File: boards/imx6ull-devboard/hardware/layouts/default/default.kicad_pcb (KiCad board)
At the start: 2 copper layers, 119 parts, among them Q1 Vgs ℝ+V

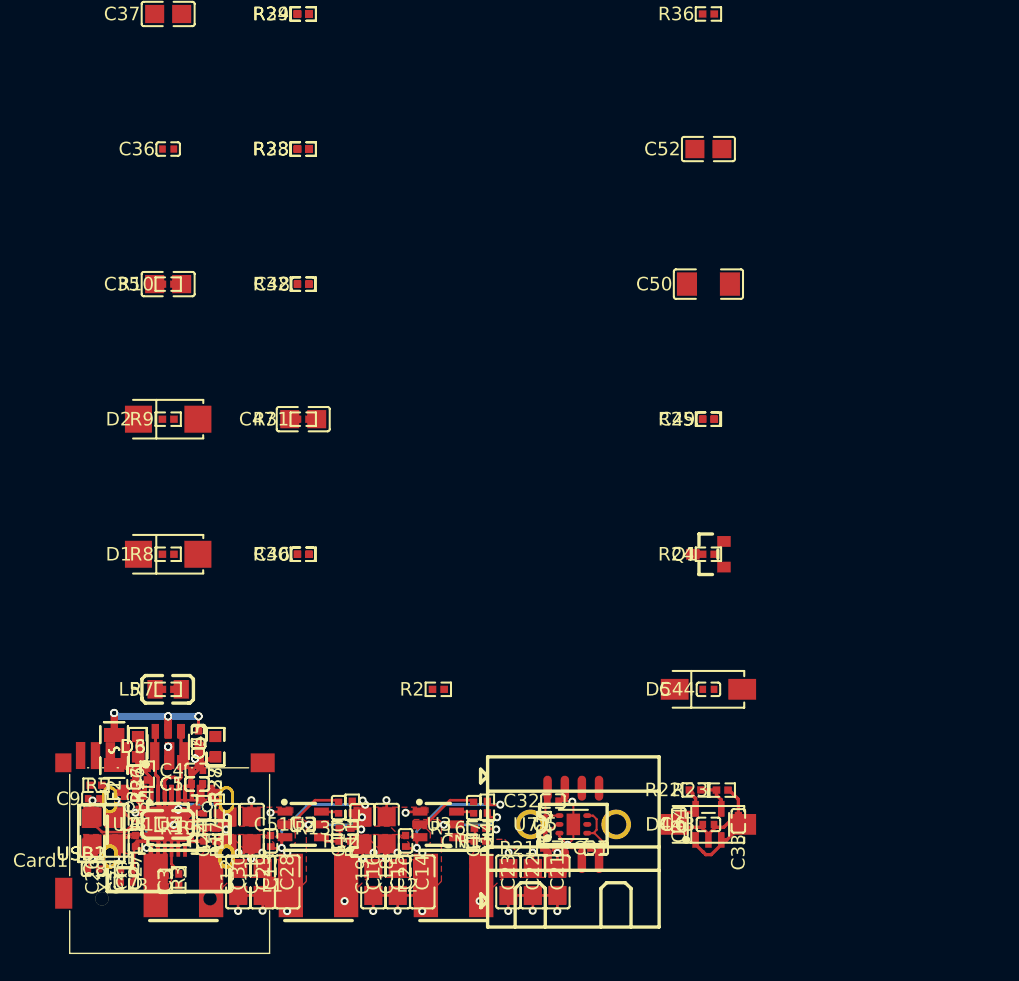
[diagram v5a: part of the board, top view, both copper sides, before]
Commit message: Debug subsystem v0 — JTAG, reset, boot DIP, LEDs, coin cell, headers
Components:
- 10-pin Cortex JTAG/SWD SMD header (Wcon, 1.27mm) with named pins
  per ARM debug spec (VTREF/SWDIO_TMS/SWCLK_TCK/SWO_TDO/TDI/NSRST/GNDs)
- SMD tactile reset button (XKB, JLC Basic) + 10kΩ pullup + 100nF debounce
- 2-position SMD DIP for BOOT_MODE[1:0] selection (kangshen DSIC02LSGET)
  with truth table documented; default position = SD boot
- 2x status LEDs (3V3 power-good always-on, MPU-driven heartbeat) via
  bridge pattern: power_3v3.hv ~> R ~> LED ~> power_3v3.lv
- CR2032 coin cell holder (Q&J) + 1kΩ charge limit → PowerTree.vbat_in
- 4-pin TTL UART header (atopile/pin-headers Male_2_54mm_1x4P_TH) for
  USB-TTL dongle fallback to MPU UART2
- 2-pin speaker header (atopile/pin-headers Male_2_54mm_1x2P_TH)

Atomic parts: added signal names to bare-pin parts (DIBO terminal block,
Wcon JTAG header, DSIC02LSGET DIP, Q&J cell holder) so they're accessible
from outside via .NAME instead of needing pin-number syntax.

Build clean. 6/9 subsystems landed.

Co-Authored-By: Claude Opus 4.7 (1M context) <noreply@anthropic.com>
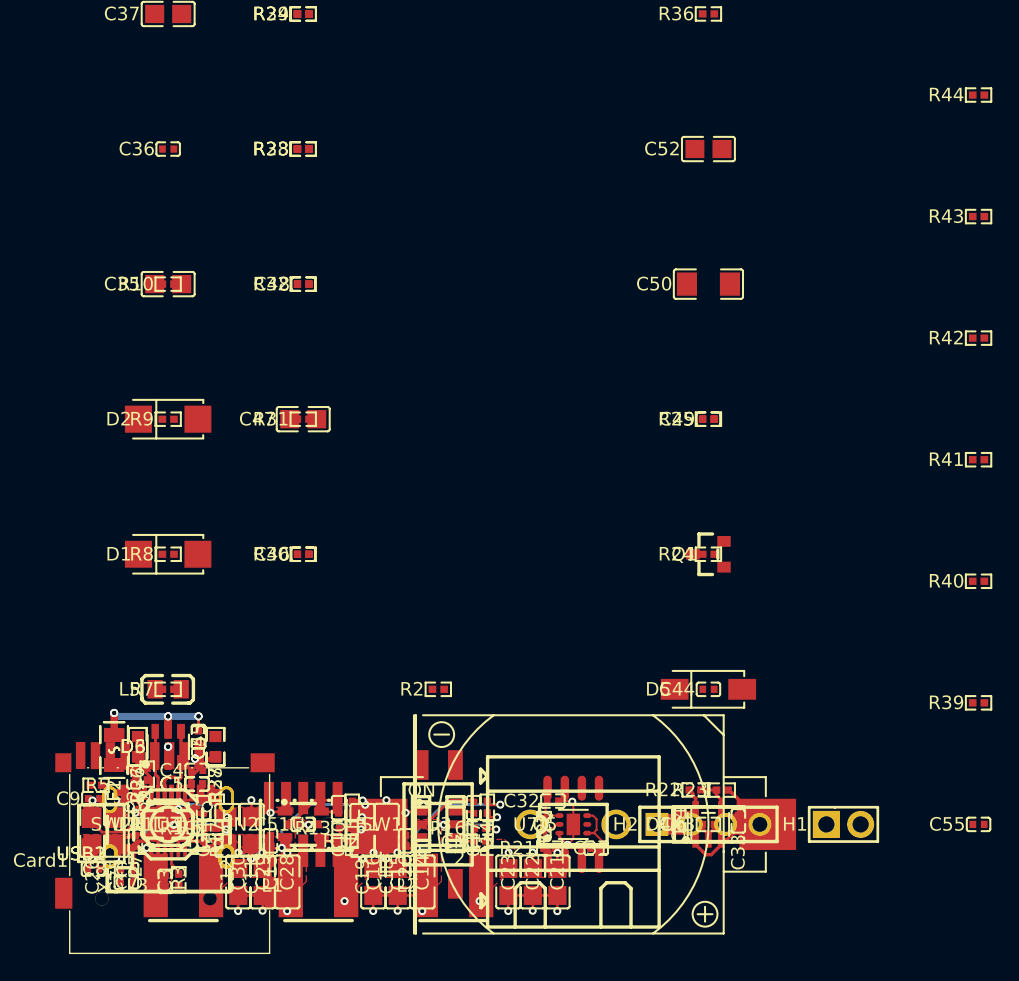
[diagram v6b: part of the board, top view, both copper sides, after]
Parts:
- added B1: , Q_J_CR2032_BS_6_1:BAT-TH_CR2032-BS-6-1, F.Cu at (30.0, 0.00)
- added C55: 100nF ±10%, Samsung_Electro_Mechanics_CL05B104KO5NNNC:C0402, F.Cu at (60.0, 0.00)
- added CN2: , Wcon_1310_1205G0M061CR02:CONN-SMD_1310-1205G0M061CR02, F.Cu at (10.0, 0.00)
- added H1: , XFCN_PZ254V_11_02P:HDR-TH_2P-P2.54-V-M, F.Cu at (50.0, 0.00)
- added H2: , Shenzhen_Kinghelm_Elec_KH_2_54PH180_1X4P_L11_5:HDR-TH_4P-P2.54-V-M, F.Cu at (40.0, 0.00)
- added R39: 10kΩ ±1%, UNI_ROYAL_0402WGF1002TCE:R0402, F.Cu at (60.0, -9.00)
- added R40: 10kΩ ±1%, UNI_ROYAL_0402WGF1002TCE:R0402, F.Cu at (60.0, -18.0)
- added R41: 1kΩ ±1%, UNI_ROYAL_0402WGF1001TCE:R0402, F.Cu at (60.0, -27.0)
- added R42: 680Ω ±1%, UNI_ROYAL_0402WGF6800TCE:R0402, F.Cu at (60.0, -36.0)
- added R43: 680Ω ±1%, UNI_ROYAL_0402WGF6800TCE:R0402, F.Cu at (60.0, -45.0)
- added R44: 10kΩ ±1%, UNI_ROYAL_0402WGF1002TCE:R0402, F.Cu at (60.0, -54.0)
- added SW1: , kangshen_DSIC02LSGET:SW-SMD_DSIC02LSGET, F.Cu at (20.0, 0.00)
- added SW2: , XKB_Connectivity_TS_1187A_B_A_B:SW-SMD_4P-L5.1-W5.1-P3.70-LS6.5-TL_H1.5, F.Cu at (0.00, 0.00)
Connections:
- net POS renamed pin_in-POS
- net anode renamed or_bench-anode
- net line renamed _reset-line
- C1 pad 2: lv -> cathode
- C11 pad 1: cathode -> power_5v-cathode
- C11 pad 2: lv -> cathode
- C12 pad 1: cathode -> power_5v-cathode
- C12 pad 2: lv -> cathode
- C13 pad 1: cathode -> power_5v-cathode
- C13 pad 2: lv -> cathode
- C14 pad 2: lv -> cathode
- C15 pad 2: lv -> cathode
- C16 pad 2: lv -> cathode
- C18 pad 1: cathode -> power_5v-cathode
- C18 pad 2: lv -> cathode
- C19 pad 1: cathode -> power_5v-cathode
- C19 pad 2: lv -> cathode
- C2 pad 2: lv -> cathode
- C20 pad 1: cathode -> power_5v-cathode
- C20 pad 2: lv -> cathode
- C21 pad 2: lv -> cathode
- C22 pad 2: lv -> cathode
- C23 pad 2: lv -> cathode
- C25 pad 1: cathode -> power_5v-cathode
- C25 pad 2: lv -> cathode
- C26 pad 1: cathode -> power_5v-cathode
- C26 pad 2: lv -> cathode
- C27 pad 1: cathode -> power_5v-cathode
- C27 pad 2: lv -> cathode
- C28 pad 2: lv -> cathode
- C29 pad 2: lv -> cathode
- C3 pad 2: lv -> cathode
- C30 pad 2: lv -> cathode
- C31 pad 2: lv -> cathode
- C33 pad 1: cathode -> power_5v-cathode
- C33 pad 2: lv -> cathode
- C34 pad 2: vbat_in-lv -> lv
- C35 pad 2: lv -> cathode
- C36 pad 2: lv -> cathode
- C37 pad 2: vbat_in-lv -> lv
- C38 pad 2: lv -> cathode
- C39 pad 2: lv -> cathode
- C4 pad 2: lv -> cathode
- C40 pad 2: lv -> cathode
- C41 pad 2: lv -> cathode
- C42 pad 2: lv -> cathode
- C43 pad 2: lv -> cathode
- C44 pad 1: cathode -> power_5v-cathode
- C44 pad 2: lv -> cathode
- C45 pad 2: lv -> cathode
- C46 pad 2: lv -> cathode
- C47 pad 2: lv -> cathode
- C48 pad 2: lv -> cathode
- C49 pad 1: cathode -> power_5v-cathode
- C49 pad 2: lv -> cathode
- C5 pad 2: lv -> cathode
- C50 pad 1: cathode -> power_5v-cathode
- C50 pad 2: lv -> cathode
- C51 pad 2: lv -> cathode
- C52 pad 1: cathode -> power_5v-cathode
- C52 pad 2: lv -> cathode
- C53 pad 2: lv -> cathode
- C54 pad 2: lv -> cathode
- C6 pad 2: lv -> cathode
- C7 pad 2: lv -> cathode
- C8 pad 2: lv -> cathode
- C9 pad 2: lv -> cathode
- CN1 pad 2: lv -> cathode
- Card1 pad 10: lv -> cathode
- Card1 pad 11: lv -> cathode
- Card1 pad 12: lv -> cathode
- Card1 pad 13: lv -> cathode
- Card1 pad 6: lv -> cathode
- D3 pad 2: lv -> cathode
- D4 pad 2: cathode -> power_5v-cathode
- D5 pad 2: cathode -> power_5v-cathode
- D6 pad 2: lv -> cathode
- R1 pad 2: lv -> cathode
- R11 pad 2: cathode -> power_5v-cathode
- R13 pad 2: lv -> cathode
- R14 pad 2: cathode -> power_5v-cathode
- R16 pad 2: lv -> cathode
- R17 pad 2: cathode -> power_5v-cathode
- R19 pad 2: lv -> cathode
- R23 pad 2: vbat_in-lv -> lv
- R26 pad 2: lv -> cathode
- R27 pad 2: lv -> cathode
- R28 pad 2: lv -> cathode
- R3 pad 2: lv -> cathode
- R36 pad 2: lv -> cathode
- R37 pad 2: lv -> cathode
- R38 pad 2: lv -> cathode
- R4 pad 2: lv -> cathode
- R5 pad 2: lv -> cathode
- U1 pad 25: lv -> cathode
- U2 pad 1: lv -> cathode
- U2 pad 3: cathode -> power_5v-cathode
- U3 pad 1: lv -> cathode
- U3 pad 3: cathode -> power_5v-cathode
- U4 pad 1: lv -> cathode
- U4 pad 3: cathode -> power_5v-cathode
- U5 pad 3: lv -> cathode
- U6 pad 1: cathode -> power_5v-cathode
- U6 pad 2: lv -> cathode
- U6 pad 3: cathode -> power_5v-cathode
- U7 pad 3: lv -> cathode
- U7 pad 5: cathode -> power_5v-cathode
- U8 pad 10: speaker_n_pad -> speaker_n
- U8 pad 11: lv -> cathode
- U8 pad 15: lv -> cathode
- U8 pad 17: lv -> cathode
- U8 pad 3: lv -> cathode
- U8 pad 9: speaker_p_pad -> speaker_p
- USB1 pad 1: lv -> cathode
- USB1 pad 12: lv -> cathode
- USB1 pad 13: lv -> cathode
- USB1 pad 14: lv -> cathode
- USB1 pad 15: lv -> cathode
- USB1 pad 16: lv -> cathode
- USB2 pad 1: lv -> cathode
- USB2 pad 12: lv -> cathode
- USB2 pad 13: lv -> cathode
- USB2 pad 14: lv -> cathode
- USB2 pad 15: lv -> cathode
- USB2 pad 16: lv -> cathode
- X1 pad 2: lv -> cathode
- X1 pad 4: lv -> cathode
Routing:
- net lv: track 21.2 -> 0.00 mm
- net cathode: track 0.00 -> 21.2 mm

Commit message: WIP: i.MX 6ULL MPU module — pinmux verified + Board wired, build blocked on picker
MPU module written with research-verified pinmux assignments (NOT guesses):
  - SAI3 on LCD_HSYNC/ENABLE/RESET (NOT SAI2 — SAI2 only muxes to JTAG or SD1
    pads on i.MX 6ULL, would kill JTAG or USDHC1)
  - MDIO/MDC on UART1_CTS_B/RTS_B (K15/J14) per imx6ul-pinfunc.h
  - SD_CD on GPIO1_IO09 (M15)
  - ETH_PHY_RESET on GPIO1_IO02 with 10kΩ pulldown (PHY held in reset until firmware)
  - JTAG_MOD via 4.7kΩ to GND (RM §59 Secure JTAG normal mode)
  - TEST_MODE via 1kΩ to GND (mandatory)
  - ONOFF + POR_B pull-ups to VDD_SNVS_IN (NOT 3V3 — SNVS-domain inputs)
  - USB_OTG1_VBUS divider (20k/30k → ~3V) per datasheet §6.4.4 protection
  - DRAM_VREF = NVCC_DRAM/2 via 1k/1k 1% divider + 100nF + 10nF filter caps
  - DRAM_ZQPAD via 240Ω 1% to GND

Board top-level wires MPU to all 7 existing subsystems:
  - PowerTree provides 4 rails (3V3, 1V4_arm, 1V4_soc, 1V35, SNVS)
  - Network/USDHC/Audio/USBUart/Debug all connected to MPU buses

DDR3 bus exposed as DDR3Bus interface; awaits DDR3 SDRAM module.

Sources cited in mpu.ato comments:
  - IMX6ULLIEC datasheet Tables 82, 94, 95
  - Mainline Linux imx6ul-pinfunc.h
  - imx6ul-14x14-evk.dtsi reference

KNOWN BLOCKER: ato build fails with picker contradiction on
  Board.psu.buck_3v3.feedback_divider.chain.resistors[0/1].resistance
even with explicit pinned R values. This is an atopile internal solver issue —
the same module compiled fine with fewer downstream consumers but the larger
constraint set (MPU + 6 other subsystems referencing power_3v3) makes the
TPS563201 package's internal feedback divider unsatisfiable.

Stopping here for user direction rather than continuing to iterate on
constraints without root-cause understanding.

Co-Authored-By: Claude Opus 4.7 (1M context) <noreply@anthropic.com>
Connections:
- R39 pad 2: hv -> power_snvs-cathode
- R40 pad 2: hv -> power_snvs-cathode
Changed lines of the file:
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@@
 	(net 50 "power_1v4_soc-hv")
 	(net 51 "_ldo_snvs_out-anode")
-	(net 54 "power_snvs-cathode")
 	(net 15 "cap_v3-power-hv")
 	(net 35 "nRTS")
@@
 	(net 108 "lv")
 	(net 109 "vbat_in-anode")
+	(net 52 "power_snvs-cathode")
 	(footprint "Microchip_Tech_LAN8742A_CZ_TR:QFN-24_L4.0-W4.0-P0.50-TL-EP2.5"
 		(layer "F.Cu")
@@
 			(size 2 2)
 			(layers "F.Cu" "F.Paste" "F.Mask")
-			(net 54 "power_snvs-cathode")
+			(net 52 "power_snvs-cathode")
 		)
 		(embedded_fonts no)
@@
 			(size 2 2)
 			(layers "F.Cu" "F.Paste" "F.Mask")
-			(net 54 "power_snvs-cathode")
+			(net 52 "power_snvs-cathode")
 		)
 		(embedded_fonts no)
@@
 			(size 1.41 1.35)
 			(layers "F.Cu" "F.Paste" "F.Mask")
-			(net 54 "power_snvs-cathode")
+			(net 52 "power_snvs-cathode")
 		)
 		(embedded_fonts no)
@@
 		)
 		(pad "" thru_hole circle
-			(at -1.9 -0 0)
+			(at -1.9 -0)
 			(size 1.05 1.05)
 			(drill 1.05)
@@
 		)
 		(pad "" thru_hole circle
-			(at 1.9 -0 0)
+			(at 1.9 -0)
 			(size 1.05 1.05)
 			(drill 1.05)
@@
 		)
 		(pad "1" thru_hole rect
-			(at -1.27 0 0)
+			(at -1.27 0)
 			(size 2 2)
 			(drill 1.199998)
@@
 		)
 		(pad "2" thru_hole circle
-			(at 1.27 0 0)
+			(at 1.27 0)
 			(size 2 2)
 			(drill 1.199998)
@@
 			(size 0.57 0.54)
 			(layers "F.Cu" "F.Paste" "F.Mask")
-			(net 39 "hv")
+			(net 52 "power_snvs-cathode")
 		)
 		(pad "1" smd rect
@@
 			(size 0.57 0.54)
 			(layers "F.Cu" "F.Paste" "F.Mask")
-			(net 39 "hv")
+			(net 52 "power_snvs-cathode")
 		)
 		(pad "1" smd rect
@@
 	(group "dbg.hdr_spk"
 		(locked no)
-		(members "8d349a68-802b-450d-bfa1-fe594642524b")
+		(members "98f623f6-ef0b-4de6-83db-48de4642524b")
 	)
 )

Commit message: 🚀 BUILD SUCCESSFUL — 58-part Linux dev board in KiCad
All 14 build stages green. 1.26 MB default.kicad_pcb generated.

Two fixes that closed the build:

1. Net name collisions (segfault → crash):
   Set explicit override_net_name on top-level rails (VCC_5V, VCC_3V3,
   VCC_1V4_ARM, VCC_1V4_SOC, VCC_NVCC_DRAM, VCC_1V8, VCC_SNVS, VBAT, GND)
   in main.ato:Board. atopile's PCB writer was crashing when auto-derived
   net names like "hv"/"lv"/"cathode" collided across modules. Explicit
   names give the writer deterministic output and the segfault disappeared.

2. Broken MPU pin numbers (29 lines):
   The auto-generated NXP_Semicon_MCIMX6Y2CVM08AB part from `ato create part`
   had 29 pin assignments missing their BGA row letter (e.g.,
   `BOOT_MODE1 ~ pin 10` instead of `pin U10`, `DRAM_DATA01 ~ pin 6`
   instead of `pin U6`). Read pages 113-122 of the IMX6ULLIEC datasheet
   (Tables 90, 91, 92) and corrected all 29 to the actual BGA coordinates:

   - BOOT_MODE1=U10, CCM_PMIC_STBY_REQ=U9
   - DRAM_DATA01=U6, ..03=U7, ..04=U8, ..07=U4, ..08=U2, ..09=U3, ..10=U5, ..11=R4
   - DRAM_RESET=G4, NVCC_DRAM (6th)=G6
   - RTC_XTALO=U11, UART3_RTS_B=G14, UART5_RX_DATA=G13
   - USB_OTG1_CHD_B=U16, USB_OTG1_DP=U15
   - USB_OTG2_DP=U13, USB_OTG2_VBUS=U12
   - 10× VSS pin row letters: R17, U14, U17, G5, M11, M10, M9, M8, G15, R5
   - CSI_DATA03 was D18 (out of bounds — BGA only goes to col 17); fixed to E1

   These were genuine errors in EasyEDA's symbol import — datasheet was the
   ground truth. With pin numbers correct, the i.MX 6ULL appears in the
   BOM as U9 with the correct BGA-289 footprint.

Final BOM: 58 line items including
  - U1: LAN8742A Ethernet PHY
  - U2/U3/U4: 3× TPS563201 buck (commonized via local fork)
  - U5: TLV75901 LDO 1V8
  - U6: LDK220 LDO SNVS
  - U7: CH340N USB-UART
  - U8: MAX98357A I2S Class-D amp
  - U9: i.MX 6ULL MCIMX6Y2CVM08AB BGA-289
  - 2× USB-C, 2× SS54 + 2× SS34 OR Schottkys, 2× USBLC6 ESD, 2× ferrite beads
  - 9× 10kΩ commonized 0402, 4× 47kΩ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
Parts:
- added C56: 10µF ±10%, Samsung_Electro_Mechanics_CL21A106KAYNNNE:C0805, F.Cu at (10.0, 0.00)
- added C57: 10µF ±10%, Samsung_Electro_Mechanics_CL21A106KAYNNNE:C0805, F.Cu at (10.0, -6.00)
- added C58: 22µF ±20%, Samsung_Electro_Mechanics_CL21A226MAQNNNE:C0805, F.Cu at (10.0, -12.0)
- added C59: 1µF ±10%, Samsung_Electro_Mechanics_CL05A105KA5NQNC:C0402, F.Cu at (10.0, -18.0)
- added C60: 10µF ±10%, Samsung_Electro_Mechanics_CL21A106KAYNNNE:C0805, F.Cu at (10.0, -24.0)
- added C61: 1µF ±10%, Samsung_Electro_Mechanics_CL05A105KA5NQNC:C0402, F.Cu at (10.0, -30.0)
- added C62: 1µF ±10%, Samsung_Electro_Mechanics_CL05A105KA5NQNC:C0402, F.Cu at (10.0, -36.0)
- added C63: 1µF ±10%, Samsung_Electro_Mechanics_CL05A105KA5NQNC:C0402, F.Cu at (10.0, -42.0)
- added C64: 1µF ±10%, Samsung_Electro_Mechanics_CL05A105KA5NQNC:C0402, F.Cu at (10.0, -48.0)
- added C65: 100nF ±10%, Samsung_Electro_Mechanics_CL05B104KO5NNNC:C0402, F.Cu at (10.0, -54.0)
- added C66: 10nF ±10%, Samsung_Electro_Mechanics_CL05B103KB5NNNC:C0402, F.Cu at (10.0, -60.0)
- added C67: 22pF ±5%, FH_0402CG220J500NT:C0402, F.Cu at (10.0, -66.0)
- added C68: 22pF ±5%, FH_0402CG220J500NT:C0402, F.Cu at (10.0, -72.0)
- added C69: 100nF ±10%, Samsung_Electro_Mechanics_CL05B104KO5NNNC:C0402, F.Cu at (10.0, -78.0)
- added C70: 100nF ±10%, Samsung_Electro_Mechanics_CL05B104KO5NNNC:C0402, F.Cu at (10.0, -90.0)
- added C71: 100nF ±10%, Samsung_Electro_Mechanics_CL05B104KO5NNNC:C0402, F.Cu at (10.0, -96.0)
- added C72: 100nF ±10%, Samsung_Electro_Mechanics_CL05B104KO5NNNC:C0402, F.Cu at (10.0, -102.0)
- added C73: 100nF ±10%, Samsung_Electro_Mechanics_CL05B104KO5NNNC:C0402, F.Cu at (10.0, -108.0)
- added C74: 100nF ±10%, Samsung_Electro_Mechanics_CL05B104KO5NNNC:C0402, F.Cu at (10.0, -114.0)
- added C75: 100nF ±10%, Samsung_Electro_Mechanics_CL05B104KO5NNNC:C0402, F.Cu at (10.0, -120.0)
- added C76: 100nF ±10%, Samsung_Electro_Mechanics_CL05B104KO5NNNC:C0402, F.Cu at (10.0, -126.0)
- added C77: 100nF ±10%, Samsung_Electro_Mechanics_CL05B104KO5NNNC:C0402, F.Cu at (10.0, -132.0)
- added C78: 100nF ±10%, Samsung_Electro_Mechanics_CL05B104KO5NNNC:C0402, F.Cu at (10.0, -138.0)
- added C79: 100nF ±10%, Samsung_Electro_Mechanics_CL05B104KO5NNNC:C0402, F.Cu at (10.0, -84.0)
- added C80: 100nF ±10%, Samsung_Electro_Mechanics_CL05B104KO5NNNC:C0402, F.Cu at (10.0, -144.0)
- added C81: 100nF ±10%, Samsung_Electro_Mechanics_CL05B104KO5NNNC:C0402, F.Cu at (10.0, -150.0)
- added C82: 100nF ±10%, Samsung_Electro_Mechanics_CL05B104KO5NNNC:C0402, F.Cu at (10.0, -156.0)
- added C83: 100nF ±10%, Samsung_Electro_Mechanics_CL05B104KO5NNNC:C0402, F.Cu at (10.0, -162.0)
- added C84: 100nF ±10%, Samsung_Electro_Mechanics_CL05B104KO5NNNC:C0402, F.Cu at (10.0, -168.0)
- added C85: 100nF ±10%, Samsung_Electro_Mechanics_CL05B104KO5NNNC:C0402, F.Cu at (10.0, -174.0)
- added C86: 100nF ±10%, Samsung_Electro_Mechanics_CL05B104KO5NNNC:C0402, F.Cu at (10.0, -180.0)
- added C87: 100nF ±10%, Samsung_Electro_Mechanics_CL05B104KO5NNNC:C0402, F.Cu at (10.0, -186.0)
- added C88: 100nF ±10%, Samsung_Electro_Mechanics_CL05B104KO5NNNC:C0402, F.Cu at (10.0, -192.0)
- added C89: 100nF ±10%, Samsung_Electro_Mechanics_CL05B104KO5NNNC:C0402, F.Cu at (10.0, -198.0)
- added C90: 100nF ±10%, Samsung_Electro_Mechanics_CL05B104KO5NNNC:C0402, F.Cu at (10.0, -204.0)
- added C91: 100nF ±10%, Samsung_Electro_Mechanics_CL05B104KO5NNNC:C0402, F.Cu at (10.0, -210.0)
- added C92: 100nF ±10%, Samsung_Electro_Mechanics_CL05B104KO5NNNC:C0402, F.Cu at (10.0, -216.0)
- added R45: 30kΩ ±1%, UNI_ROYAL_0402WGF3002TCE:R0402, F.Cu at (10.0, -258.0)
- added R46: 20kΩ ±1%, UNI_ROYAL_0402WGF2002TCE:R0402, F.Cu at (10.0, -264.0)
- added R47: 1kΩ ±1%, UNI_ROYAL_0402WGF1001TCE:R0402, F.Cu at (10.0, -270.0)
- added R48: 1kΩ ±1%, UNI_ROYAL_0402WGF1001TCE:R0402, F.Cu at (10.0, -276.0)
- added R49: 240Ω ±1%, YAGEO_RC0402FR_07240RL:R0402, F.Cu at (10.0, -282.0)
- added R50: 10kΩ ±1%, UNI_ROYAL_0402WGF1002TCE:R0402, F.Cu at (10.0, -300.0)
- added R51: 8.2kΩ ±1%, UNI_ROYAL_0402WGF8201TCE:R0402, F.Cu at (10.0, -306.0)
- added R52: 10kΩ ±1%, UNI_ROYAL_0402WGF1002TCE:R0402, F.Cu at (10.0, -288.0)
- added R53: 7.5kΩ ±1%, UNI_ROYAL_0402WGF7501TCE:R0402, F.Cu at (10.0, -294.0)
- added R54: 10kΩ ±1%, UNI_ROYAL_0402WGF1002TCE:R0402, F.Cu at (10.0, -312.0)
- added R55: 33kΩ ±1%, UNI_ROYAL_0402WGF3302TCE:R0402, F.Cu at (10.0, -318.0)
- added U9: , NXP_Semicon_MCIMX6Y2CVM08AB:BGA-289_L14.0-W14.0-R17-C17-P0.80-BL, F.Cu at (0.00, 0.00)
- C14, C15, C16, C21, C22, C23, C28, C29, C30: value 10µF ±10% -> 100nF ±10%; footprint Samsung_Electro_Mechanics_CL21A106KAYNNNE:C0805 -> YAGEO_CC0603KRX7R9BB104:C0603
- L1, L2, L3: value L 1.54-2.86µH -> L 2.2µH ±20%; footprint SXN_SMNR5030_2R2N:IND-SMD_L5.0-W5.0_SMNR5030 -> cjiang_FXL0420_2R2_M:IND-SMD_L4.4-W4.2
- R12: value 13.3kΩ ±1% -> 4.7kΩ ±1%; footprint FOJAN_FRC0402F1332TS:R0402 -> UNI_ROYAL_0402WGF4701TCE:R0402
- R13, R15: value 16.2kΩ ±1% -> 10kΩ ±1%; footprint UNI_ROYAL_0402WGF1622TCE:R0402 -> UNI_ROYAL_0402WGF1002TCE:R0402
- R16: value 21.5kΩ ±1% -> 10kΩ ±1%; footprint UNI_ROYAL_0402WGF2152TCE:R0402 -> UNI_ROYAL_0402WGF1002TCE:R0402
- R18: value 10.2kΩ ±1% -> 1kΩ ±1%; footprint UNI_ROYAL_0402WGF1022TCE:R0402 -> UNI_ROYAL_0402WGF1001TCE:R0402
- R19: value 3.09kΩ ±1% -> 10kΩ ±1%; footprint Viking_Tech_ARG02FTC3091:R0402 -> UNI_ROYAL_0402WGF1002TCE:R0402
- moved R19 252.4 mm to (10.0, -252.0)
- moved R18 247.3 mm to (10.0, -246.0), turned to 0 degrees
- moved R16 240.6 mm to (10.0, -240.0)
- moved R15 235.6 mm to (10.0, -234.0), turned to 0 degrees
- moved R13 228.3 mm to (10.0, -228.0)
- moved R12 223.3 mm to (10.0, -222.0), turned to 0 degrees
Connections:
- net MDIO renamed UART1_RTS_B
- B1 pad 2: lv -> cathode
- C1 pad 1: hv -> power_3v3-cathode
- C11 pad 1: power_5v-cathode -> input_caps[0]-power-hv-1
- C11 pad 2: cathode -> input_caps[0]-power-lv-1
- C12 pad 1: power_5v-cathode -> input_caps[1]-power-hv-1
- C12 pad 2: cathode -> input_caps[1]-power-lv-1
- C13 pad 1: power_5v-cathode -> input_caps[2]-power-hv-1
- C13 pad 2: cathode -> input_caps[2]-power-lv-1
- C14 pad 1: power_1v4_arm-hv -> output_caps[0]-power-hv-1
- C14 pad 2: cathode -> output_caps[0]-power-lv-1
- C15 pad 1: power_1v4_arm-hv -> output_caps[1]-power-hv-1
- C15 pad 2: cathode -> output_caps[1]-power-lv-1
- C16 pad 1: power_1v4_arm-hv -> output_caps[2]-power-hv-1
- C16 pad 2: cathode -> output_caps[2]-power-lv-1
- C18 pad 1: power_5v-cathode -> input_caps[0]-power-hv
- C18 pad 2: cathode -> input_caps[0]-power-lv
- C19 pad 1: power_5v-cathode -> input_caps[1]-power-hv
- C19 pad 2: cathode -> input_caps[1]-power-lv
- C2 pad 1: hv -> power_3v3-cathode
- C20 pad 1: power_5v-cathode -> input_caps[2]-power-hv
- C20 pad 2: cathode -> input_caps[2]-power-lv
- C21 pad 1: _buck_1v35_out-hv -> output_caps[0]-power-hv
- C21 pad 2: cathode -> output_caps[0]-power-lv
- C22 pad 1: _buck_1v35_out-hv -> output_caps[1]-power-hv
- C22 pad 2: cathode -> output_caps[1]-power-lv
- C23 pad 1: _buck_1v35_out-hv -> output_caps[2]-power-hv
- C23 pad 2: cathode -> output_caps[2]-power-lv
- C25 pad 1: power_5v-cathode -> input_caps[0]-power-hv-2
- C25 pad 2: cathode -> input_caps[0]-power-lv-2
- C26 pad 1: power_5v-cathode -> input_caps[1]-power-hv-2
- C26 pad 2: cathode -> input_caps[1]-power-lv-2
- C27 pad 1: power_5v-cathode -> input_caps[2]-power-hv-2
- C27 pad 2: cathode -> input_caps[2]-power-lv-2
- C28 pad 1: hv -> output_caps[0]-power-hv-2
- C28 pad 2: cathode -> output_caps[0]-power-lv-2
- C29 pad 1: hv -> output_caps[1]-power-hv-2
- C29 pad 2: cathode -> output_caps[1]-power-lv-2
- C3 pad 1: hv -> power_3v3-cathode
- C30 pad 1: hv -> output_caps[2]-power-hv-2
- C30 pad 2: cathode -> output_caps[2]-power-lv-2
- C31 pad 1: hv -> power_3v3-cathode
- C32 pad 2: power_1v8-lv -> lv
- C34 pad 2: lv -> cathode
- C37 pad 1: power_snvs-cathode -> power_3v3-cathode
- C37 pad 2: lv -> cathode
- C4 pad 1: hv -> power_3v3-cathode
- C43 pad 1: cap_v3-power-hv -> hv
- C46 pad 1: hv -> power_3v3-cathode
- C47 pad 1: hv -> power_3v3-cathode
- C48 pad 1: hv -> power_3v3-cathode
- C5 pad 1: hv -> power_3v3-cathode
- C51 pad 1: hv -> power_3v3-cathode
- C54 pad 1: hv -> power_3v3-cathode
- CN2 pad 1: hv -> power_3v3-cathode
- Card1 pad 4: hv -> power_3v3-cathode
- D1 pad 1: power_snvs-cathode -> power_3v3-cathode
- D2 pad 1: power_snvs-cathode -> power_3v3-cathode
- H2 pad 2: hv -> power_3v3-cathode
- H2 pad 3: uart_console-TX -> TX
- H2 pad 4: uart_console-RX -> RX
- L3 pad 2: hv -> power_3v3-cathode
- R10 pad 2: hv -> power_3v3-cathode
- R12 pad 1: power_1v4_arm-hv -> JTAG_MOD
- R12 pad 2: feedback_divider-ref_out-hv-1 -> cathode
- R13 pad 1: feedback_divider-ref_out-hv-1 -> ONOFF
- R13 pad 2: cathode -> power_3v3-cathode
- R15 pad 1: _buck_1v35_out-hv -> _reset-line
- R15 pad 2: feedback_divider-ref_out-hv -> cathode
- R16 pad 1: feedback_divider-ref_out-hv -> c_rst_db-power-hv
- R16 pad 2: cathode -> power_3v3-cathode
- R18 pad 1: hv -> TEST_MODE
- R18 pad 2: feedback_divider-ref_out-hv-2 -> cathode
- R19 pad 1: feedback_divider-ref_out-hv-2 -> N_TRST
- R19 pad 2: cathode -> power_3v3-cathode
- R2 pad 2: hv -> power_3v3-cathode
- R20 pad 2: feedback_divider-ref_out-hv-3 -> feedback_divider-ref_out-hv
- R21 pad 1: feedback_divider-ref_out-hv-3 -> feedback_divider-ref_out-hv
- R21 pad 2: power_1v8-lv -> lv
- R22 pad 2: feedback_divider-ref_out-hv-4 -> feedback_divider-ref_out-hv-1
- R23 pad 1: feedback_divider-ref_out-hv-4 -> feedback_divider-ref_out-hv-1
- R23 pad 2: lv -> cathode
- R29 pad 2: hv -> power_3v3-cathode
- R3 pad 1: phy-rmii-line -> ENET1_RX_ER
- R30 pad 2: hv -> power_3v3-cathode
- R31 pad 2: hv -> power_3v3-cathode
- R32 pad 2: hv -> power_3v3-cathode
- R33 pad 2: hv -> power_3v3-cathode
- R34 pad 2: hv -> power_3v3-cathode
- R35 pad 2: hv -> power_3v3-cathode
- R39 pad 2: power_snvs-cathode -> power_3v3-cathode
- R40 pad 2: power_snvs-cathode -> power_3v3-cathode
- R43 pad 1: hv -> power_3v3-cathode
- R44 pad 2: hv -> power_3v3-cathode
- R6 pad 2: hv -> power_3v3-cathode
- R7 pad 2: hv -> power_3v3-cathode
- R8 pad 2: hv -> power_3v3-cathode
- R9 pad 2: hv -> power_3v3-cathode
- U1 pad 1: hv -> power_3v3-cathode
- U1 pad 10: phy-rmii-line -> ENET1_RX_ER
- U1 pad 11: phy-rmii-line-1 -> ENET1_RX_EN
- U1 pad 13: MDC -> UART1_CTS_B
- U1 pad 14: nINT_REFCLKO -> ENET1_TX_CLK
- U1 pad 16: TXEN -> ENET1_TX_EN
- U1 pad 17: phy-rmii-line-2 -> phy-rmii-line-1
- U1 pad 18: phy-rmii-line-3 -> phy-rmii-line
- U1 pad 19: hv -> power_3v3-cathode
- U1 pad 7: phy-rmii-line-4 -> phy-rmii-line-2
- U1 pad 8: phy-rmii-line-5 -> phy-rmii-line-3
- U1 pad 9: hv -> power_3v3-cathode
- U2 pad 4: feedback_divider-ref_out-hv-1 -> psu.buck_1v4-VFB
- U3 pad 4: feedback_divider-ref_out-hv -> VFB
- U4 pad 4: feedback_divider-ref_out-hv-2 -> psu.buck_3v3-VFB
- U5 pad 2: feedback_divider-ref_out-hv-3 -> feedback_divider-ref_out-hv
- U5 pad 4: hv -> power_3v3-cathode
- U5 pad 6: hv -> power_3v3-cathode
- U5 pad 7: power_1v8-lv -> lv
- U6 pad 4: feedback_divider-ref_out-hv-4 -> feedback_divider-ref_out-hv-1
- U7 pad 8: cap_v3-power-hv -> hv
- U8 pad 7: hv -> power_3v3-cathode
- U8 pad 8: hv -> power_3v3-cathode
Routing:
- net bootstrap_cap-power-lv: track 0.00 -> 56.2 mm, vias 0 -> 23
- net SD: track 56.2 -> 0.00 mm, vias 23 -> 0
- net input_caps[0]-power-lv: track 0.00 -> 21.2 mm
- net cathode: track 21.2 -> 0.00 mm
- net cap_v3-power-hv: track 5.89 -> 0.00 mm, vias 2 -> 0
- net output_caps[2]-power-hv-1: track 0.00 -> 4.83 mm
- net WS: track 4.83 -> 0.00 mm
- net UART5_RX_DATA: track 0.00 -> 3.86 mm
- net feedback_divider-ref_out-hv-3: track 2.65 -> 0.00 mm
- net feedback_divider-ref_out-hv: track 0.00 -> 2.65 mm
- net hv: track 3.86 -> 5.89 mm, vias 0 -> 2
- net phy-rmii-line: track 1.89 -> 0.00 mm
- net output_caps[0]-power-lv-2: track 0.00 -> 1.89 mm
- net output_caps[0]-power-hv-1: track 0.00 -> 1.11 mm
- net _reset-line: track 1.11 -> 0.00 mm
